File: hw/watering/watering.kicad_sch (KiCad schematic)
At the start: 7 parts, among them J2 USB_C_Receptacle

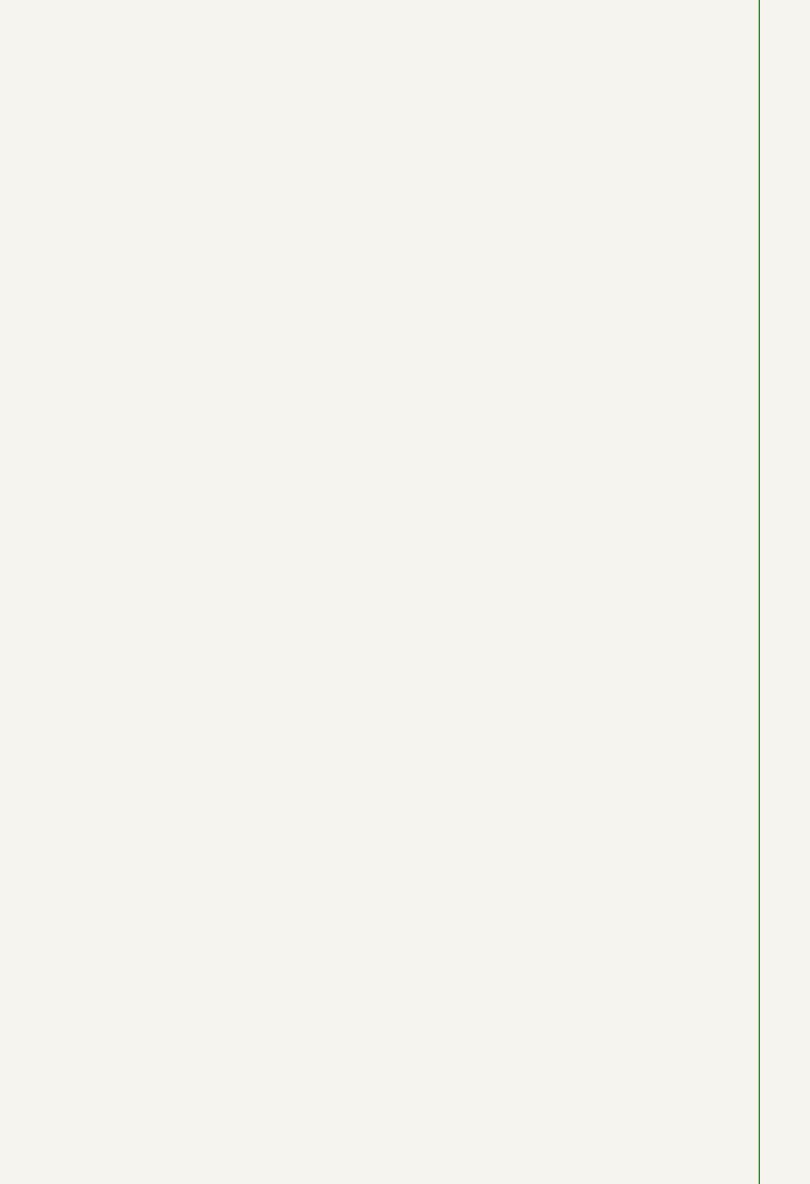
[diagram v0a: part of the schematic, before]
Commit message: - improved voltage boost on battery power - some issues with rtc clock - some issues with pwm that result in brownout
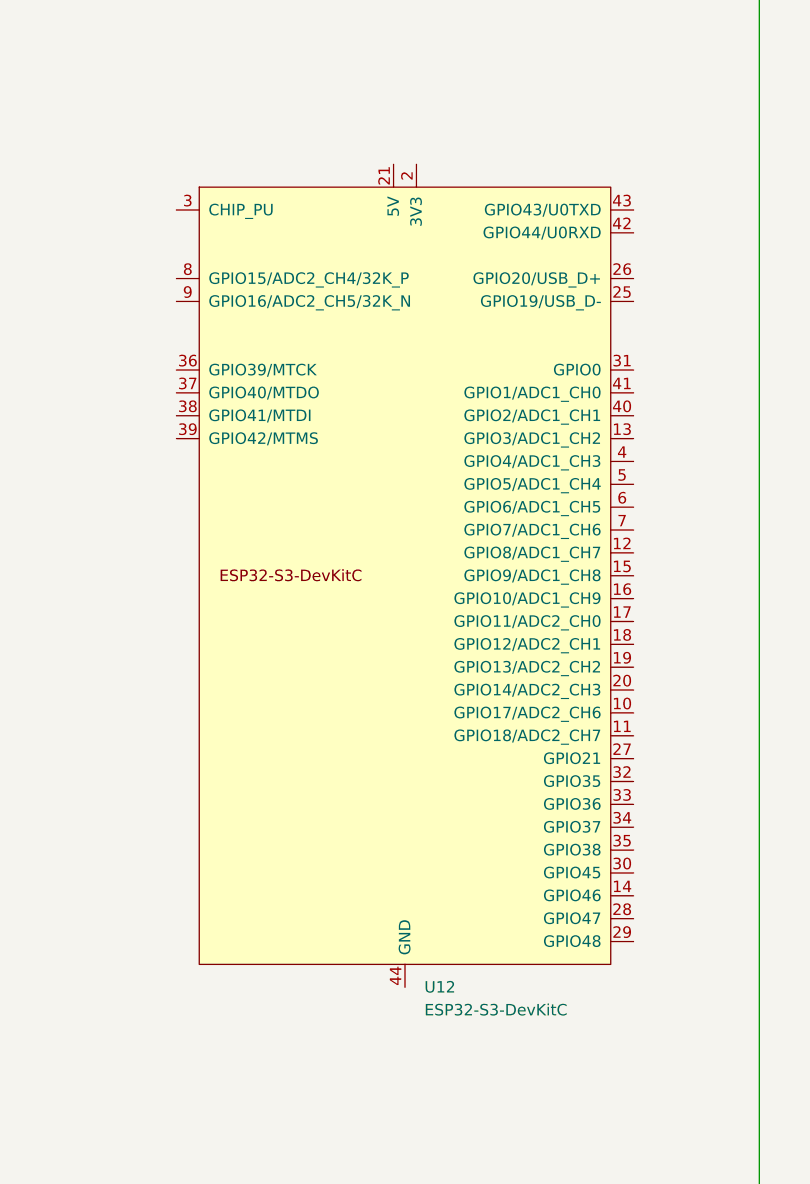
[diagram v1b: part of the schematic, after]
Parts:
- added U12: ESP32-S3-DevKitC, PCM_Espressif:ESP32-S3-DevKitC, symbol PCM_Espressif:ESP32-S3-DevKitC
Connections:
- new net: U12.1 (3V3), U12.2 (3V3)
- new net: U12.22 (GND), U12.23 (GND), U12.24 (GND), U12.44 (GND)
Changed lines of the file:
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@@
+	)
+	(symbol
+		(lib_id "PCM_Espressif:ESP32-S3-DevKitC")
+		(at 175.26 102.87 0)
+		(unit 1)
+		(body_style 1)
+		(exclude_from_sim no)
+		(in_bom yes)
+		(on_board yes)
+		(in_pos_files yes)
+		(dnp no)
+		(fields_autoplaced yes)
+		(property "Reference" "U12"
+			(at 177.4033 148.59 0)
+			(show_name no)
+			(do_not_autoplace no)
+			(effects
+				(font
+					(size 1.27 1.27)
+				)
+				(justify left)
+			)
+		)
+		(property "Value" "ESP32-S3-DevKitC"
+			(at 177.4033 151.13 0)
+			(show_name no)
+			(do_not_autoplace no)
+			(effects
+				(font
+					(size 1.27 1.27)
+				)
+				(justify left)
+			)
+		)
+		(property "Footprint" "PCM_Espressif:ESP32-S3-DevKitC"
+			(at 175.26 160.02 0)
+			(hide yes)
+			(show_name no)
+			(do_not_autoplace no)
+			(effects
+				(font
+					(size 1.27 1.27)
+				)
+			)
+		)
+		(property "Datasheet" ""
+			(at 115.57 105.41 0)
+			(hide yes)
+			(show_name no)
+			(do_not_autoplace no)
+			(effects
+				(font
+					(size 1.27 1.27)
+				)
+			)
+		)
+		(property "Description" "ESP32-S3-DevKitC"
+			(at 175.26 102.87 0)
+			(hide yes)
+			(show_name no)
+			(do_not_autoplace no)
+			(effects
+				(font
+					(size 1.27 1.27)
+				)
+			)
+		)
+		(pin "7"
+		)
+		(pin "19"
+		)
+		(pin "39"
+		)
+		(pin "40"
+		)
+		(pin "31"
+		)
+		(pin "1"
+		)
+		(pin "43"
+		)
+		(pin "42"
+		)
+		(pin "5"
+		)
+		(pin "2"
+		)
+		(pin "44"
+		)
+		(pin "41"
+		)
+		(pin "14"
+		)
+		(pin "4"
+		)
+		(pin "34"
+		)
+		(pin "38"
+		)
+		(pin "3"
+		)
+		(pin "29"
+		)
+		(pin "6"
+		)
+		(pin "37"
+		)
+		(pin "22"
+		)
+		(pin "21"
+		)
+		(pin "20"
+		)
+		(pin "18"
+		)
+		(pin "17"
+		)
+		(pin "16"
+		)
+		(pin "15"
+		)
+		(pin "13"
+		)
+		(pin "12"
+		)
+		(pin "11"
+		)
+		(pin "10"
+		)
+		(pin "28"
+		)
+		(pin "24"
+		)
+		(pin "27"
+		)
+		(pin "26"
+		)
+		(pin "23"
+		)
+		(pin "9"
+		)
+		(pin "25"
+		)
+		(pin "33"
+		)
+		(pin "35"
+		)
+		(pin "32"
+		)
+		(pin "8"
+		)
+		(pin "30"
+		)
+		(pin "36"
+		)
+		(instances
+			(project "watering"
+				(path "/cfeeaa6f-be25-403f-b03c-39be367d5a74"
+					(reference "U12")
+					(unit 1)
+				)
+			)
+		)
 	)
 	(symbol

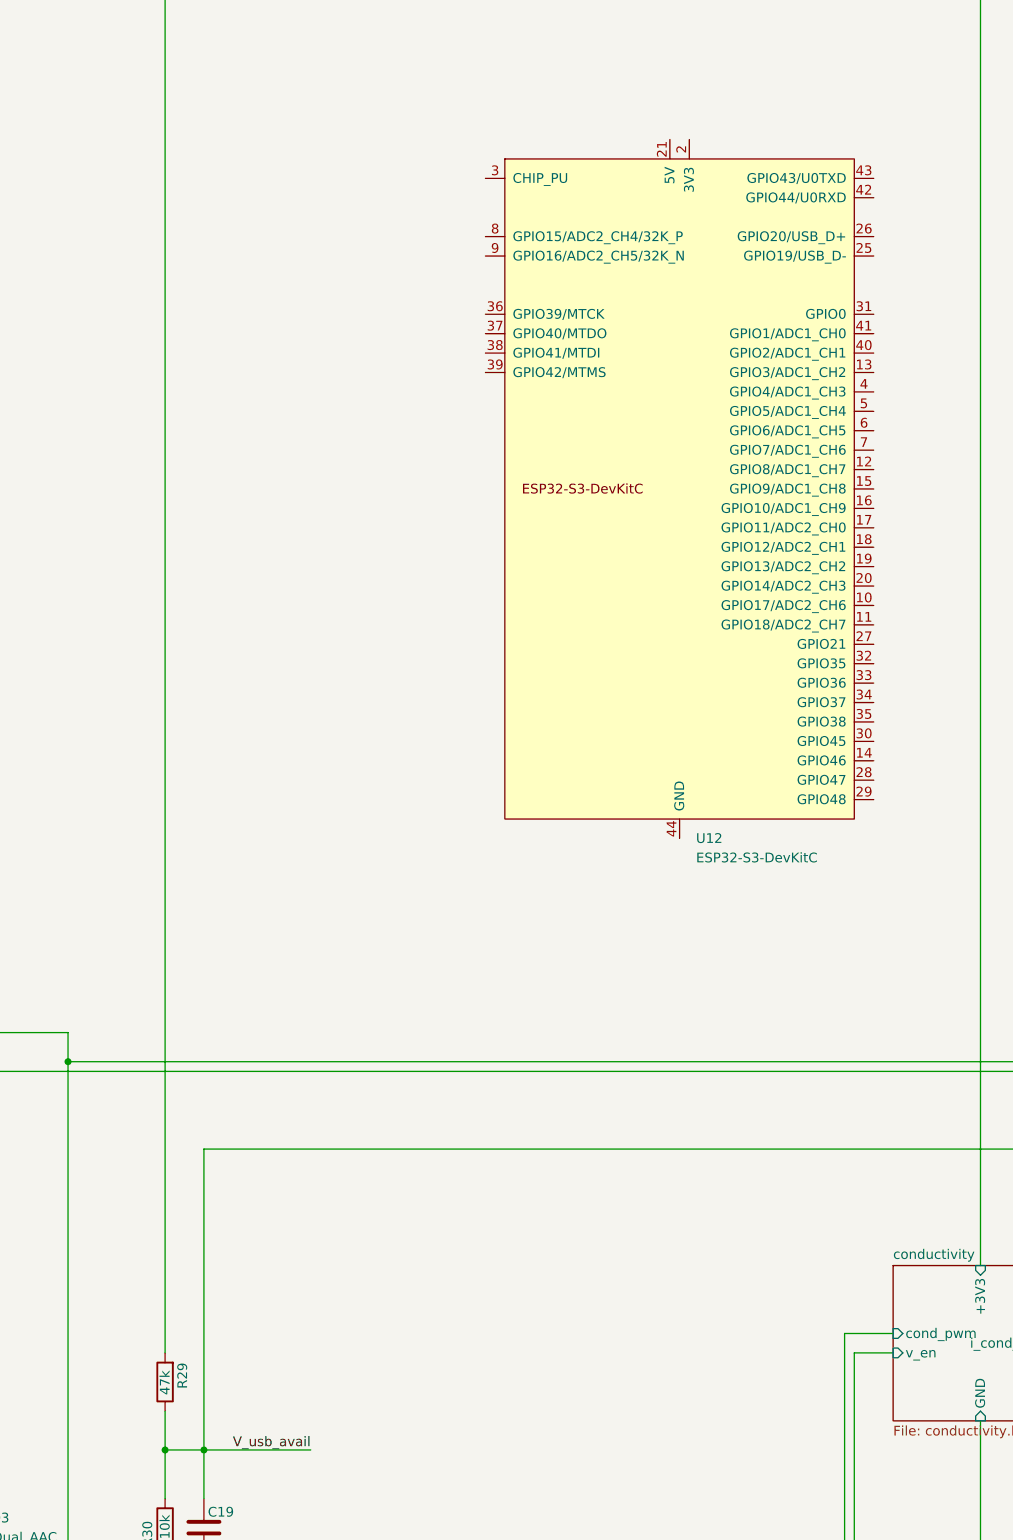
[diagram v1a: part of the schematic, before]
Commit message: - fixed formatting - proper pwm output for conductivity output
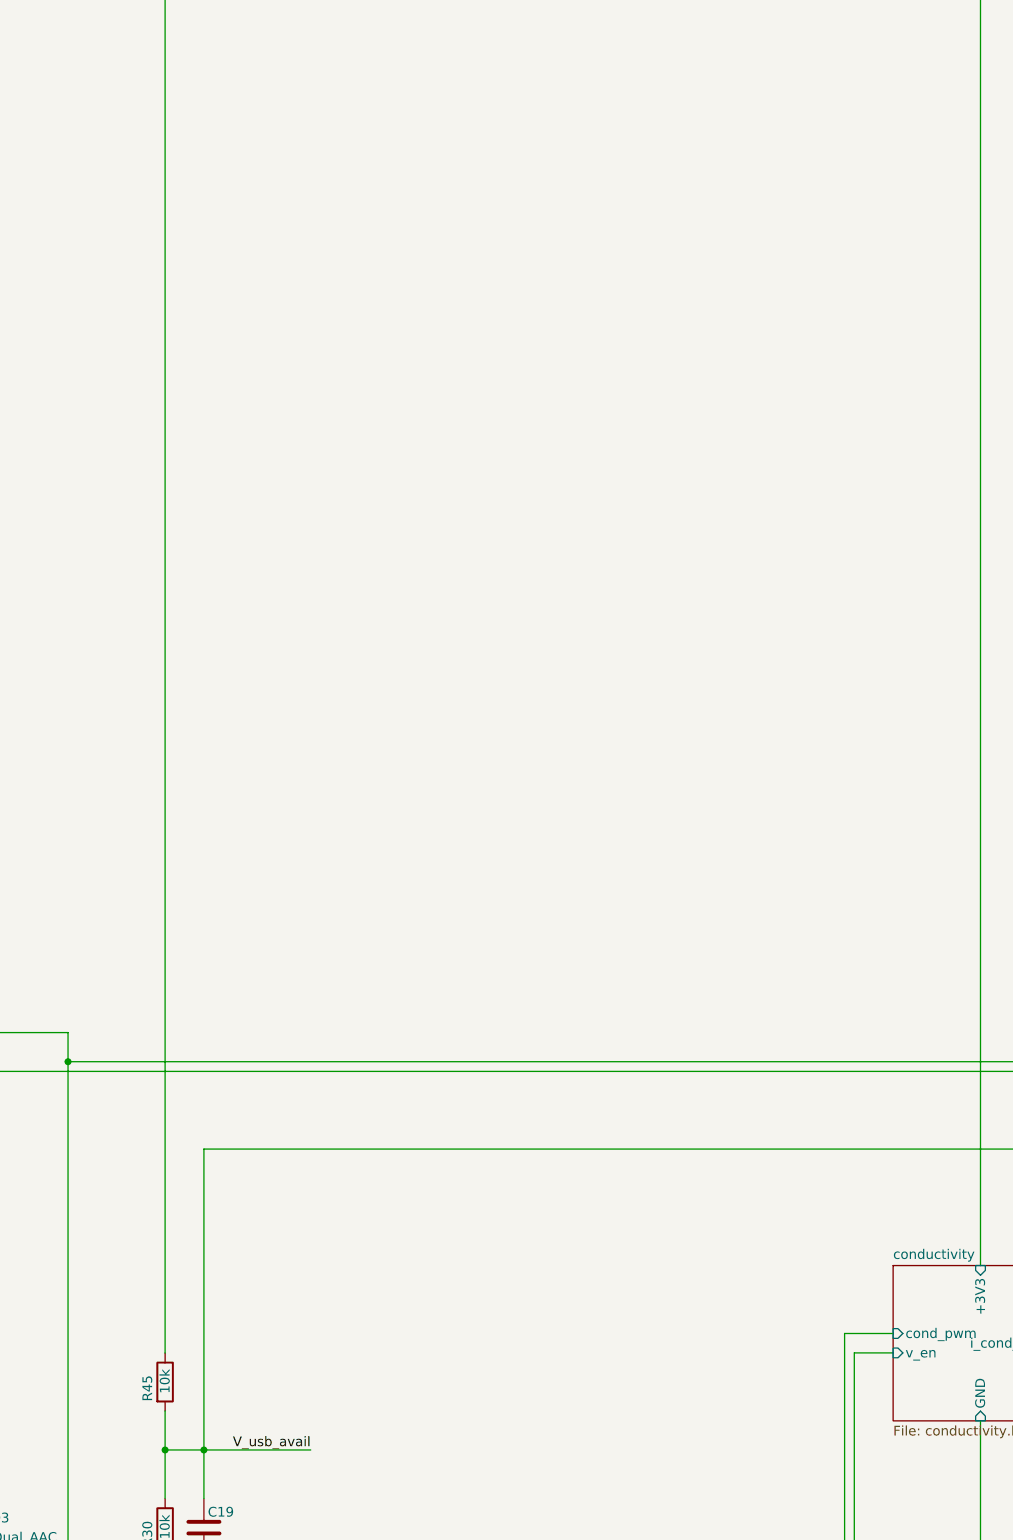
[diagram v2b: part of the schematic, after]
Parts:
- removed R29: 47k, Resistor_SMD:R_0603_1608Metric, symbol Device:R
- removed U12: ESP32-S3-DevKitC, PCM_Espressif:ESP32-S3-DevKitC, symbol PCM_Espressif:ESP32-S3-DevKitC
- added R45: 10k, Resistor_SMD:R_0603_1608Metric, symbol Device:R
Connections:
- net +5V: now also R45.1
- net V_usb_avail: now also R45.2
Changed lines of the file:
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@@
 	)
 	(symbol
-		(lib_id "PCM_Espressif:ESP32-S3-DevKitC")
-		(at 175.26 102.87 0)
+		(lib_id "Device:R")
+		(at 107.95 219.71 0)
 		(unit 1)
 		(body_style 1)
@@
 		(in_pos_files yes)
 		(dnp no)
-		(fields_autoplaced yes)
-		(property "Reference" "U12"
-			(at 177.4033 148.59 0)
+		(property "Reference" "R45"
+			(at 105.664 222.25 90)
 			(show_name no)
 			(do_not_autoplace no)
@@
 			)
 		)
-		(property "Value" "ESP32-S3-DevKitC"
-			(at 177.4033 151.13 0)
+		(property "Value" "10k"
+			(at 107.95 221.234 90)
 			(show_name no)
 			(do_not_autoplace no)
@@
 			)
 		)
-		(property "Footprint" "PCM_Espressif:ESP32-S3-DevKitC"
-			(at 175.26 160.02 0)
+		(property "Footprint" "Resistor_SMD:R_0603_1608Metric"
+			(at 106.172 219.71 90)
 			(hide yes)
 			(show_name no)
@@
 			)
 		)
-		(property "Datasheet" ""
-			(at 115.57 105.41 0)
+		(property "Datasheet" "https://jlc-prod-smt.oss-eu-central-1.aliyuncs.com/smtDataManualFile/8579706381316128768-C25804.pdf?response-content-disposition=attachment%3B%20filename%3DC25804.pdf%3B%20filename%2A%3DUTF-8%27%27C25804.pdf&x-oss-date=20260604T182440Z&x-oss-expires=1800&x-oss-security-token=CAISgAN1q6Ft5B2yfSjIr5nhDvTiu55L8aayRHLFsEERZtthpKj%2B0Dz2IHhMdHJsAOodtv0%2FmmhT6PkclqRLcbhpcmfjV%2BZHzLB8qeRniENA4J7b16cNrbH4M4H6aXeirtuwDsz9SNTCALjPD3nPii50x5bjaDymRCbLGJaViJlhHLN1Ow6jdmhpCctxLAlvo9NgFxm3D%2Fu2NQPwiWf9FVdhvhEG6Vly8qOi2MaRmFy8yFTx0b0SvJ%2BjYMrmPctoN9JnSdC5mfdzau3a1TJ84gRD0a5wkaVA1zbDs5bfISEIuUzebreLqY03dV4mOvdqIcMe8qigz88fk%2FfIioH6xyxKOexoSCnFTOiiupCcQLPyao9jLu6iayqViY7QaIOTqQohZmkAMwVOasAsI3Ngh4zF97Qt0cVNkXO9gWfLI8DtuMleWhri1Udu3tHD0eS19jklBdzSlusJRAJJUVBflCeKEaRNSAd3WGhEfM2%2BBt4QT30w5N2u00S8OSMIOONBvqKWD5sagAGpldF62iBeHzrNV%2BHnUyjaA64BCjacRbVbSjmxSgiuNX1d%2FbCnqQV25prdqNhtDbAKCoRnNQDFNxmhLIIUUcffM9eG3oRc44RNhyi7hADN6z1ILjt6TEoRuXkDAYH1u8iyrE2YQDMkq7F3Cke8dxQ44PYZqWefci6GHDzQ1pzPpiAA&x-oss-signature-version=OSS4-HMAC-SHA256&x-oss-credential=STS.NZTENVVAjFdYFTtTADjTMKmU2%2F20260604%2Feu-central-1%2Foss%2Faliyun_v4_request&x-oss-signature=78c2b620008555fdaf271c3d0b7682edd0aca7d23428d31f63338848e1713cab"
+			(at 107.95 219.71 0)
 			(hide yes)
 			(show_name no)
@@
 			)
 		)
-		(property "Description" "ESP32-S3-DevKitC"
-			(at 175.26 102.87 0)
+		(property "Description" "C25804"
+			(at 107.95 219.71 0)
 			(hide yes)
 			(show_name no)
@@
 			)
 		)
-		(pin "7"
-		)
-		(pin "19"
-		)
-		(pin "39"
-		)
-		(pin "40"
-		)
-		(pin "31"
-		)
 		(pin "1"
 		)
-		(pin "43"
-		)
-		(pin "42"
-		)
-		(pin "5"
-		)
 		(pin "2"
-		)
-		(pin "44"
-		)
-		(pin "41"
-		)
-		(pin "14"
-		)
-		(pin "4"
-		)
-		(pin "34"
-		)
-		(pin "38"
-		)
-		(pin "3"
-		)
-		(pin "29"
-		)
-		(pin "6"
-		)
-		(pin "37"
-		)
-		(pin "22"
-		)
-		(pin "21"
-		)
-		(pin "20"
-		)
-		(pin "18"
-		)
-		(pin "17"
-		)
-		(pin "16"
-		)
-		(pin "15"
-		)
-		(pin "13"
-		)
-		(pin "12"
-		)
-		(pin "11"
-		)
-		(pin "10"
-		)
-		(pin "28"
-		)
-		(pin "24"
-		)
-		(pin "27"
-		)
-		(pin "26"
-		)
-		(pin "23"
-		)
-		(pin "9"
-		)
-		(pin "25"
-		)
-		(pin "33"
-		)
-		(pin "35"
-		)
-		(pin "32"
-		)
-		(pin "8"
-		)
-		(pin "30"
-		)
-		(pin "36"
 		)
 		(instances
 			(project "watering"
 				(path "/cfeeaa6f-be25-403f-b03c-39be367d5a74"
-					(reference "U12")
+					(reference "R45")
 					(unit 1)
 				)
@@
 					(unit 1)
 				)
-			)
-		)
-	)
-	(symbol
-		(lib_id "Device:R")
-		(at 107.95 219.71 180)
-		(unit 1)
-		(body_style 1)
-		(exclude_from_sim no)
-		(in_bom yes)
-		(on_board yes)
-		(in_pos_files yes)
-		(dnp no)
-		(property "Reference" "R29"
-			(at 110.236 217.17 90)
-			(show_name no)
-			(do_not_autoplace no)
-			(effects
-				(font
-					(size 1.27 1.27)
-				)
-				(justify left)
-			)
-		)
-		(property "Value" "47k"
-			(at 107.95 218.186 90)
-			(show_name no)
-			(do_not_autoplace no)
-			(effects
-				(font
-					(size 1.27 1.27)
-				)
-				(justify left)
-			)
-		)
-		(property "Footprint" "Resistor_SMD:R_0603_1608Metric"
-			(at 109.728 219.71 90)
-			(hide yes)
-			(show_name no)
-			(do_not_autoplace no)
-			(effects
-				(font
-					(size 1.27 1.27)
-				)
-			)
-		)
-		(property "Datasheet" "https://jlc-prod-smt.oss-eu-central-1.aliyuncs.com/smtDataManualFile/8579706364622934016-C25819.pdf?response-content-disposition=attachment%3B%20filename%3DC25819.pdf%3B%20filename%2A%3DUTF-8%27%27C25819.pdf&x-oss-date=20260607T210642Z&x-oss-expires=1800&x-oss-security-token=CAISgAN1q6Ft5B2yfSjIr5ryH8PCprRbhIysal7ylzcBXuxKqZznuzz2IHhMdHJsAOodtv0%2FmmhT6PkclqRLcbhpcmfjV%2BZHzLB8qbxek0BD4J7b16cNrbH4M4H6aXeirtuwDsz9SNTCALjPD3nPii50x5bjaDymRCbLGJaViJlhHLN1Ow6jdmhpCctxLAlvo9NgFxm3D%2Fu2NQPwiWf9FVdhvhEG6Vly8qOi2MaRmFy8yFTx0b0SvJ%2BjYMrmPctoN9JnSdC5mfdzau3a1TJ84gRD0a5wkaVA1zbDs5bfISEIuUzebreLqY03dV4mOvdqIcMe8qigz88fk%2FfIioH6xyxKOexoSCnFTOiiupCcQLPyao9jLu6iayqViY7QaIOTqQohZmkAMwVOasAsI3Ngh4zF97Qt0cVNkXO9gWfLI8DtuMleWkpjUPw8wnSgc5lCkRRYwGs1287ugXlSQzo890KPDAEovaKCnZ2ZSfh7Y4sNknI6i%2Bfc2Se2MIkIuzN54aKWD5sagAFXqr37yeC6i73JtnWyrAPWlFlD7%2BO4v6D0kklJkfR4ZNWYY%2FJmHaMvh5XgKe69Y2VVwh3FQXeQc9N3YnYUCwlUFj7ysfoRU0zIPvuKAhEOT3qEObty6yli3txhJK%2BkEcQ4NQs%2FlNRRqPdiq%2BB4j8AoteNyHTVnRr3qFmKb96GmHCAA&x-oss-signature-version=OSS4-HMAC-SHA256&x-oss-credential=STS.NYGTyvKkz3NGhxCs7TRcfFYLY%2F20260607%2Feu-central-1%2Foss%2Faliyun_v4_request&x-oss-signature=d302d6996d62a00132e559a883be9b5fca7841b1eb7e44c91ba09bae985432b1"
-			(at 107.95 219.71 0)
-			(hide yes)
-			(show_name no)
-			(do_not_autoplace no)
-			(effects
-				(font
-					(size 1.27 1.27)
-				)
-			)
-		)
-		(property "Description" "C25819"
-			(at 107.95 219.71 0)
-			(hide yes)
-			(show_name no)
-			(do_not_autoplace no)
-			(effects
-				(font
-					(size 1.27 1.27)
-				)
-			)
-		)
-		(pin "1"
-		)
-		(pin "2"
-		)
-		(instances
-			(project "watering"
-				(path "/cfeeaa6f-be25-403f-b03c-39be367d5a74"
-					(reference "R29")
-					(unit 1)
-				)
